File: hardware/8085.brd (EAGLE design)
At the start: 167.9 x 122.5 mm, 54 parts, among them IC10 74HCT00N, IC11 74HCT245DW, IC2 74AC573N, IC3 ATF16V8BP3, IC4 74AC00D, IC5 74HCT245DW, IC6 74AC273N, IC7 74HCT139N, IC8 7404N, IC9 74HCT138N

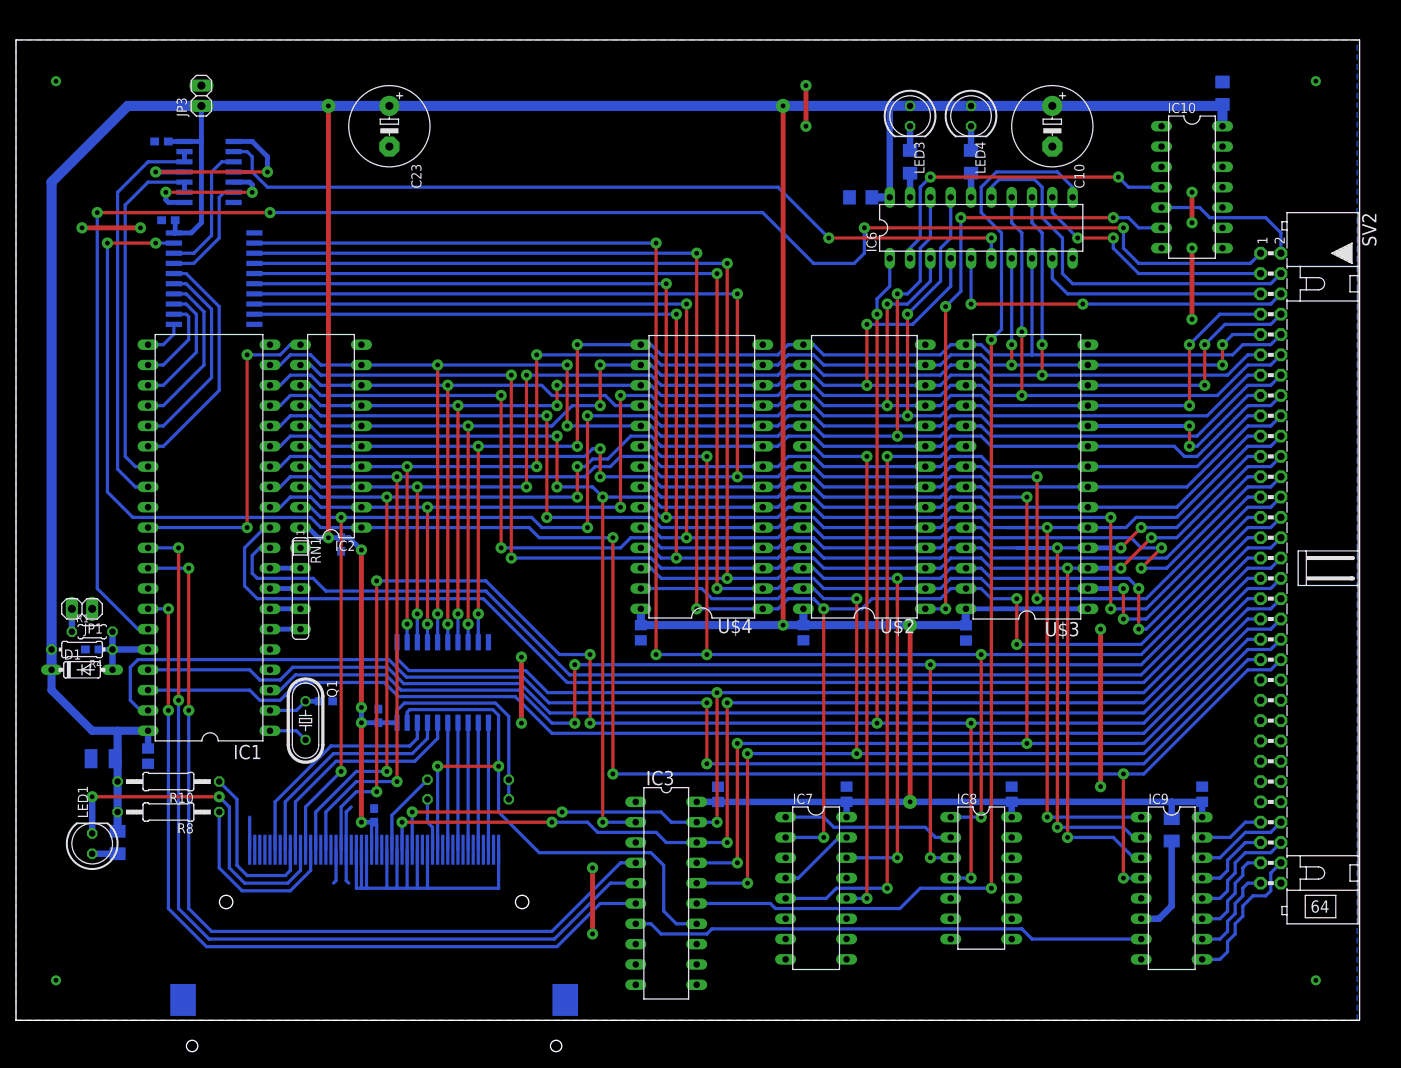
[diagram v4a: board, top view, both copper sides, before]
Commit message: IO address decoder gated with IOM signal
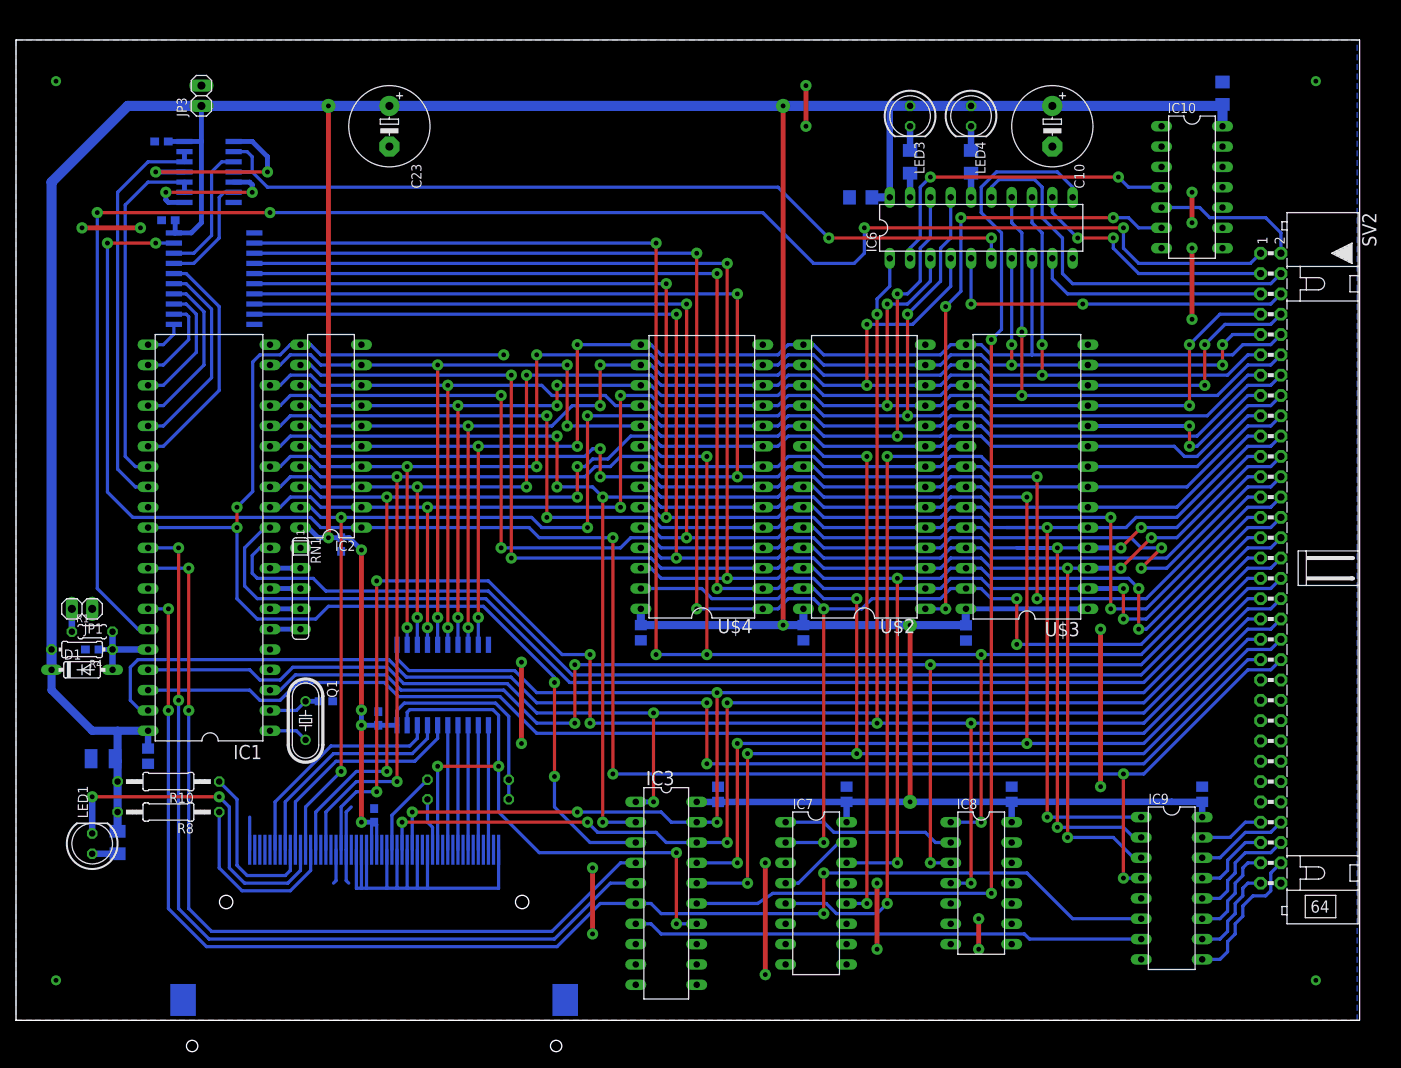
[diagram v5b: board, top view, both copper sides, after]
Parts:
- removed R9: 10k, rcl:M1206
- moved IC7 0.64 mm to (100.0, 15.9)
- moved IC8 0.64 mm to (120.7, 17.1)
- moved C5 0.32 mm to (45.3, 37.7)
- moved IC11 0.32 mm to (53.3, 41.9)
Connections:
- removed net N$20: IC9.6, R9.1
- net ALE: now also IC3.3
- net CLK: now also IC3.1
- net GND: no longer IC3.3
- net IO_M: now also IC9.6
- net VCC: no longer R9.2
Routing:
- net ALE: track 41.2 -> 147.6 mm, vias 2 -> 5
- net IO_M: track 102.6 -> 173.8 mm, vias 2 -> 4
- net GND: track 140.7 -> 168.6 mm, vias 14 -> 20
- net CLK: track 151.1 -> 164.4 mm, vias 0 -> 2
- net N$20: track 12.6 -> 0.00 mm
- net CS_EPROM: track 77.6 -> 80.0 mm
- net CF_CS0: track 77.2 -> 79.4 mm, vias 2 -> 4
- net RESET: track 166.6 -> 167.2 mm
- net A14: track 217.4 -> 218.1 mm
- net CS_RAM2: track 66.2 -> 66.9 mm
- net A15: track 243.5 -> 244.1 mm
- net A13: track 233.8 -> 234.4 mm
- net !RESET: track 245.9 -> 246.5 mm
- net LOCAL_IO_CS: track 64.5 -> 64.0 mm

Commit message: minor PCB change
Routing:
- net IO_M: track 173.8 -> 173.0 mm
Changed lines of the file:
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@@
 <wire x1="77.47" y1="14.605" x2="79.375" y2="14.605" width="0.4064" layer="16"/>
 <wire x1="79.375" y1="14.605" x2="80.645" y2="13.335" width="0.4064" layer="16"/>
-<wire x1="80.645" y1="13.335" x2="100.965" y2="13.335" width="0.4064" layer="16"/>
-<via x="100.965" y="13.335" extent="1-16" drill="0.6" diameter="1.4224" shape="octagon"/>
-<wire x1="100.965" y1="13.335" x2="100.965" y2="18.415" width="0.4064" layer="1"/>
-<via x="100.965" y="18.415" extent="1-16" drill="0.6" diameter="1.4224" shape="octagon"/>
-<wire x1="100.965" y1="18.415" x2="126.365" y2="18.415" width="0.4064" layer="16"/>
+<wire x1="80.645" y1="13.335" x2="100.6475" y2="13.335" width="0.4064" layer="16"/>
+<via x="100.6475" y="13.335" extent="1-16" drill="0.6" diameter="1.4224" shape="octagon"/>
+<via x="100.6475" y="17.145" extent="1-16" drill="0.6" diameter="1.4224" shape="octagon"/>
 <wire x1="126.365" y1="18.415" x2="132.08" y2="12.7" width="0.4064" layer="16"/>
 <wire x1="132.08" y1="12.7" x2="140.6525" y2="12.7" width="0.4064" layer="16"/>
+<wire x1="126.365" y1="18.415" x2="101.9175" y2="18.415" width="0.4064" layer="16"/>
+<wire x1="101.9175" y1="18.415" x2="100.6475" y2="17.145" width="0.4064" layer="16"/>
+<wire x1="100.6475" y1="13.335" x2="100.6475" y2="17.145" width="0.4064" layer="1"/>
 </signal>
 <signal name="LOCAL_PORT_CS">

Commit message: Another minor PCB update
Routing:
- net GND: track 168.6 -> 159.7 mm, vias 20 -> 18
- net IO_M: track 173.0 -> 166.6 mm, vias 4 -> 2
- net LOCAL_PORT_CS: track 141.3 -> 140.2 mm
- net CS_EPROM: track 80.0 -> 78.9 mm, vias 2 -> 4
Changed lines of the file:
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@@
 <via x="93.6625" y="5.715" extent="1-16" drill="0.6" diameter="1.4224" shape="octagon"/>
 <wire x1="93.6625" y1="19.685" x2="93.6625" y2="5.715" width="0.6096" layer="1"/>
-<via x="120.3325" y="12.7" extent="1-16" drill="0.6" diameter="1.4224" shape="octagon"/>
-<via x="120.3325" y="8.89" extent="1-16" drill="0.6" diameter="1.4224" shape="octagon"/>
-<wire x1="120.3325" y1="12.7" x2="120.3325" y2="8.89" width="0.6096" layer="1"/>
-<via x="107.6325" y="17.145" extent="1-16" drill="0.6" diameter="1.4224" shape="octagon"/>
-<via x="107.6325" y="8.89" extent="1-16" drill="0.6" diameter="1.4224" shape="octagon"/>
-<wire x1="107.6325" y1="17.145" x2="107.6325" y2="8.89" width="0.6096" layer="1"/>
+<via x="120.65" y="12.065" extent="1-16" drill="0.6" diameter="1.4224" shape="octagon"/>
+<via x="120.65" y="8.89" extent="1-16" drill="0.6" diameter="1.4224" shape="octagon"/>
+<wire x1="120.65" y1="12.065" x2="120.65" y2="8.89" width="0.6096" layer="1"/>
 </signal>
 <signal name="D0">
@@
 <wire x1="115.57" y1="70.485" x2="108.9025" y2="70.485" width="0.4064" layer="16"/>
 <via x="108.9025" y="70.485" extent="1-16" drill="0.6" diameter="1.4224" shape="octagon"/>
-<via x="108.9025" y="14.605" extent="1-16" drill="0.6" diameter="1.4224" shape="octagon"/>
-<wire x1="108.9025" y1="14.605" x2="108.9025" y2="70.485" width="0.4064" layer="1"/>
+<via x="108.9025" y="18.415" extent="1-16" drill="0.6" diameter="1.4224" shape="octagon"/>
+<wire x1="108.9025" y1="18.415" x2="108.9025" y2="70.485" width="0.4064" layer="1"/>
 <contactref element="IC7" pad="5"/>
-<wire x1="101.2825" y1="14.605" x2="96.2025" y2="14.605" width="0.4064" layer="16"/>
-<wire x1="101.2825" y1="14.605" x2="102.5525" y2="13.335" width="0.4064" layer="16"/>
-<wire x1="102.5525" y1="13.335" x2="107.6325" y2="13.335" width="0.4064" layer="16"/>
-<wire x1="107.6325" y1="13.335" x2="108.9025" y2="14.605" width="0.4064" layer="16"/>
+<wire x1="100.965" y1="14.605" x2="96.2025" y2="14.605" width="0.4064" layer="16"/>
+<wire x1="108.9025" y1="18.415" x2="100.965" y2="18.415" width="0.4064" layer="16"/>
+<via x="100.965" y="18.415" extent="1-16" drill="0.6" diameter="1.4224" shape="octagon"/>
+<wire x1="100.965" y1="18.415" x2="100.965" y2="14.605" width="0.4064" layer="1"/>
+<via x="100.965" y="14.605" extent="1-16" drill="0.6" diameter="1.4224" shape="octagon"/>
 </signal>
 <signal name="OUT_4">
@@
 <wire x1="77.47" y1="14.605" x2="79.375" y2="14.605" width="0.4064" layer="16"/>
 <wire x1="79.375" y1="14.605" x2="80.645" y2="13.335" width="0.4064" layer="16"/>
-<wire x1="80.645" y1="13.335" x2="100.6475" y2="13.335" width="0.4064" layer="16"/>
-<via x="100.6475" y="13.335" extent="1-16" drill="0.6" diameter="1.4224" shape="octagon"/>
-<via x="100.6475" y="17.145" extent="1-16" drill="0.6" diameter="1.4224" shape="octagon"/>
-<wire x1="126.365" y1="18.415" x2="132.08" y2="12.7" width="0.4064" layer="16"/>
-<wire x1="132.08" y1="12.7" x2="140.6525" y2="12.7" width="0.4064" layer="16"/>
-<wire x1="126.365" y1="18.415" x2="101.9175" y2="18.415" width="0.4064" layer="16"/>
-<wire x1="101.9175" y1="18.415" x2="100.6475" y2="17.145" width="0.4064" layer="16"/>
-<wire x1="100.6475" y1="13.335" x2="100.6475" y2="17.145" width="0.4064" layer="1"/>
+<wire x1="127" y1="12.7" x2="140.6525" y2="12.7" width="0.4064" layer="16"/>
+<wire x1="80.645" y1="13.335" x2="126.365" y2="13.335" width="0.4064" layer="16"/>
+<wire x1="126.365" y1="13.335" x2="127" y2="12.7" width="0.4064" layer="16"/>
 </signal>
 <signal name="LOCAL_PORT_CS">
 <contactref element="IC6" pad="11"/>
 <contactref element="IC3" pad="15"/>
-<via x="121.92" y="15.875" extent="1-16" drill="0.6" diameter="1.4224" shape="octagon"/>
+<via x="121.92" y="17.78" extent="1-16" drill="0.6" diameter="1.4224" shape="octagon"/>
 <wire x1="132.08" y1="102.87" x2="132.08" y2="104.14" width="0.4064" layer="16"/>
 <wire x1="132.08" y1="104.14" x2="130.175" y2="106.045" width="0.4064" layer="16"/>
@@
 <wire x1="120.65" y1="100.965" x2="123.19" y2="98.425" width="0.4064" layer="16"/>
 <wire x1="123.19" y1="98.425" x2="123.19" y2="86.36" width="0.4064" layer="16"/>
-<wire x1="121.92" y1="15.875" x2="121.92" y2="85.09" width="0.4064" layer="1"/>
+<wire x1="121.92" y1="17.78" x2="121.92" y2="85.09" width="0.4064" layer="1"/>
 <via x="121.92" y="85.09" extent="1-16" drill="0.6" diameter="1.4224" shape="octagon"/>
 <wire x1="123.19" y1="86.36" x2="121.92" y2="85.09" width="0.4064" layer="16"/>
 <wire x1="85.09" y1="14.605" x2="92.71" y2="14.605" width="0.4064" layer="16"/>
 <wire x1="92.71" y1="14.605" x2="94.615" y2="15.875" width="0.4064" layer="16"/>
-<wire x1="94.615" y1="15.875" x2="121.92" y2="15.875" width="0.4064" layer="16"/>
+<wire x1="94.615" y1="15.875" x2="120.015" y2="15.875" width="0.4064" layer="16"/>
+<wire x1="120.015" y1="15.875" x2="121.92" y2="17.78" width="0.4064" layer="16"/>
 </signal>
 <signal name="N$3">
